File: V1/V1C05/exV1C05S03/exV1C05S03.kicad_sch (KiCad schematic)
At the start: 4 parts

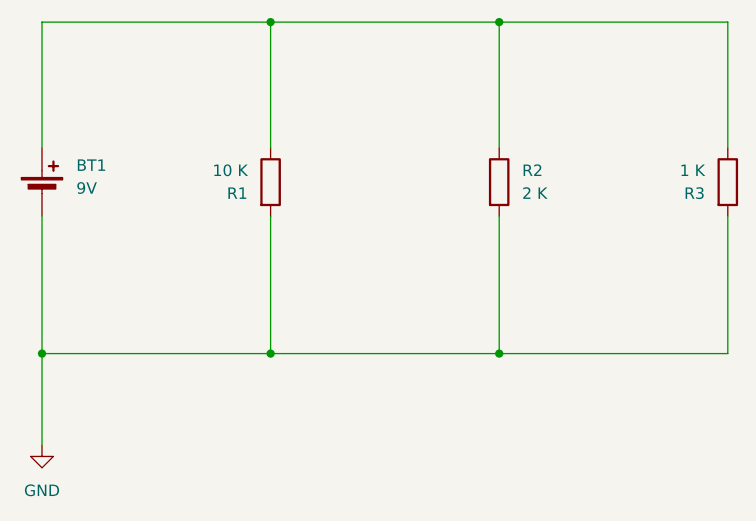
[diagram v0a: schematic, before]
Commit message: update V1 C05 C06 C07
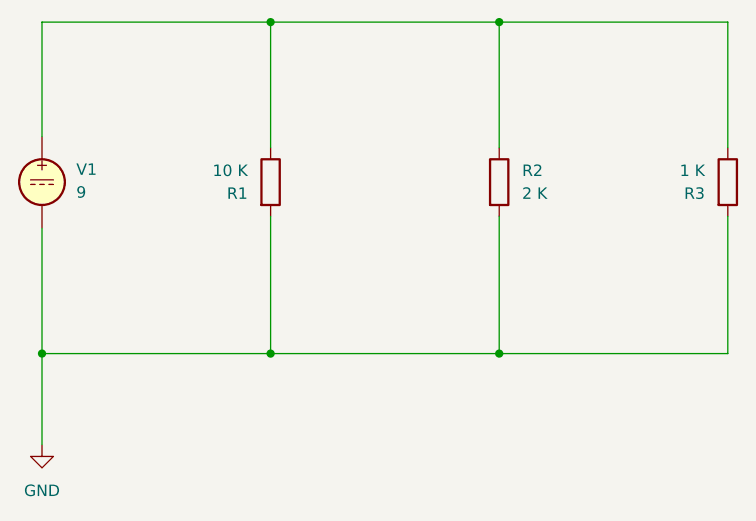
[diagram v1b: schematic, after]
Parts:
- removed BT1: 9V, symbol Device:Battery_Cell
- added V1: 9, symbol Simulation_SPICE:VDC
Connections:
- net GND: now also V1.2
- net at R1.1, R2.1, R3.1: now also V1.1
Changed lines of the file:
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@@
+	)
+	(junction
+		(at 165.1 101.6)
+		(diameter 0)
+		(color 0 0 0 0)
+	)
+	(junction
+		(at 165.1 64.77)
+		(diameter 0)
+		(color 0 0 0 0)
 	)
 	(junction
@@
 	)
 	(junction
-		(at 165.1 101.6)
-		(diameter 0)
-		(color 0 0 0 0)
-	)
-	(junction
-		(at 165.1 64.77)
-		(diameter 0)
-		(color 0 0 0 0)
-	)
-	(junction
 		(at 139.7 64.77)
 		(diameter 0)
@@
 	(wire
 		(pts
-			(xy 114.3 86.36) (xy 114.3 101.6)
-		)
-		(stroke
-			(width 0)
-			(type default)
-		)
-	)
-	(wire
-		(pts
 			(xy 165.1 86.36) (xy 165.1 101.6)
 		)
@@
 	(wire
 		(pts
+			(xy 114.3 64.77) (xy 114.3 77.47)
+		)
+		(stroke
+			(width 0)
+			(type default)
+		)
+	)
+	(wire
+		(pts
+			(xy 114.3 87.63) (xy 114.3 101.6)
+		)
+		(stroke
+			(width 0)
+			(type default)
+		)
+	)
+	(wire
+		(pts
 			(xy 139.7 64.77) (xy 165.1 64.77)
 		)
@@
 		(pts
 			(xy 165.1 64.77) (xy 190.5 64.77)
-		)
-		(stroke
-			(width 0)
-			(type default)
-		)
-	)
-	(wire
-		(pts
-			(xy 114.3 64.77) (xy 114.3 78.74)
 		)
 		(stroke
@@
 	)
 	(symbol
+		(lib_id "Simulation_SPICE:VDC")
+		(at 114.3 82.55 0)
+		(unit 1)
+		(body_style 1)
+		(exclude_from_sim no)
+		(in_bom yes)
+		(on_board yes)
+		(in_pos_files yes)
+		(dnp no)
+		(fields_autoplaced yes)
+		(property "Reference" "V1"
+			(at 118.11 81.1501 0)
+			(show_name no)
+			(do_not_autoplace no)
+			(effects
+				(font
+					(size 1.27 1.27)
+				)
+				(justify left)
+			)
+		)
+		(property "Value" "9"
+			(at 118.11 83.6901 0)
+			(show_name no)
+			(do_not_autoplace no)
+			(effects
+				(font
+					(size 1.27 1.27)
+				)
+				(justify left)
+			)
+		)
+		(property "Footprint" ""
+			(at 114.3 82.55 0)
+			(hide yes)
+			(show_name no)
+			(do_not_autoplace no)
+			(effects
+				(font
+					(size 1.27 1.27)
+				)
+			)
+		)
+		(property "Datasheet" "https://ngspice.sourceforge.io/docs/ngspice-html-manual/manual.xhtml#sec_Independent_Sources_for"
+			(at 114.3 82.55 0)
+			(hide yes)
+			(show_name no)
+			(do_not_autoplace no)
+			(effects
+				(font
+					(size 1.27 1.27)
+				)
+			)
+		)
+		(property "Description" "Voltage source, DC"
+			(at 114.3 82.55 0)
+			(hide yes)
+			(show_name no)
+			(do_not_autoplace no)
+			(effects
+				(font
+					(size 1.27 1.27)
+				)
+			)
+		)
+		(property "Sim.Pins" "1=+ 2=-"
+			(at 114.3 82.55 0)
+			(hide yes)
+			(show_name no)
+			(do_not_autoplace no)
+			(effects
+				(font
+					(size 1.27 1.27)
+				)
+			)
+		)
+		(property "Sim.Type" "DC"
+			(at 114.3 82.55 0)
+			(hide yes)
+			(show_name no)
+			(do_not_autoplace no)
+			(effects
+				(font
+					(size 1.27 1.27)
+				)
+			)
+		)
+		(property "Sim.Device" "V"
+			(at 114.3 82.55 0)
+			(hide yes)
+			(show_name no)
+			(do_not_autoplace no)
+			(effects
+				(font
+					(size 1.27 1.27)
+				)
+				(justify left)
+			)
+		)
+		(pin "1"
+		)
+		(pin "2"
+		)
+		(instances
+			(project "exV1C05S03"
+				(path "/aac4f3a6-14a3-4da2-8c20-38f6484893a9"
+					(reference "V1")
+					(unit 1)
+				)
+			)
+		)
+	)
+	(symbol
 		(lib_id "Device:R")
 		(at 190.5 82.55 0)
@@
 					(unit 1)
 				)
-			)
-		)
-	)
-	(symbol
-		(lib_id "Device:Battery_Cell")
-		(at 114.3 83.82 0)
-		(unit 1)
-		(body_style 1)
-		(exclude_from_sim no)
-		(in_bom yes)
-		(on_board yes)
-		(in_pos_files yes)
-		(dnp no)
-		(fields_autoplaced yes)
-		(property "Reference" "BT1"
-			(at 118.11 80.7084 0)
-			(show_name no)
-			(do_not_autoplace no)
-			(effects
-				(font
-					(size 1.27 1.27)
-				)
-				(justify left)
-			)
-		)
-		(property "Value" "9V"
-			(at 118.11 83.2484 0)
-			(show_name no)
-			(do_not_autoplace no)
-			(effects
-				(font
-					(size 1.27 1.27)
-				)
-				(justify left)
-			)
-		)
-		(property "Footprint" ""
-			(at 114.3 82.296 90)
-			(hide yes)
-			(show_name no)
-			(do_not_autoplace no)
-			(effects
-				(font
-					(size 1.27 1.27)
-				)
-			)
-		)
-		(property "Datasheet" ""
-			(at 114.3 82.296 90)
-			(hide yes)
-			(show_name no)
-			(do_not_autoplace no)
-			(effects
-				(font
-					(size 1.27 1.27)
-				)
-			)
-		)
-		(property "Description" "Single-cell battery"
-			(at 114.3 83.82 0)
-			(hide yes)
-			(show_name no)
-			(do_not_autoplace no)
-			(effects
-				(font
-					(size 1.27 1.27)
-				)
-			)
-		)
-		(property "Sim.Device" "V"
-			(at 114.3 83.82 0)
-			(hide yes)
-			(show_name no)
-			(do_not_autoplace no)
-			(effects
-				(font
-					(size 1.27 1.27)
-				)
-			)
-		)
-		(property "Sim.Type" "DC"
-			(at 114.3 83.82 0)
-			(hide yes)
-			(show_name no)
-			(do_not_autoplace no)
-			(effects
-				(font
-					(size 1.27 1.27)
-				)
-			)
-		)
-		(property "Sim.Pins" "1=+ 2=-"
-			(at 114.3 83.82 0)
-			(hide yes)
-			(show_name no)
-			(do_not_autoplace no)
-			(effects
-				(font
-					(size 1.27 1.27)
-				)
-			)
-		)
-		(property "Sim.Params" "dc=9"
-			(at 114.3 83.82 0)
-			(hide yes)
-			(show_name no)
-			(do_not_autoplace no)
-			(effects
-				(font
-					(size 1.27 1.27)
-				)
-			)
-		)
-		(pin "1"
-		)
-		(pin "2"
-		)
-		(instances
-			(project "exV1C05S03"
-				(path "/aac4f3a6-14a3-4da2-8c20-38f6484893a9"
-					(reference "BT1")
-					(unit 1)
-				)
